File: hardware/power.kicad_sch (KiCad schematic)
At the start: 39 parts, among them J2 USB4110-GF-A, J3 B2B-PH-K-S, J4 PRPC001DAAN-RC, J5 PRPC001DAAN-RC, J6 PRPC001DAAN-RC, Q1 IRLML2246TRPBF, U1 USBLC6-2SC6, U2 BQ24074RGT, U3 TLV76733DGNR

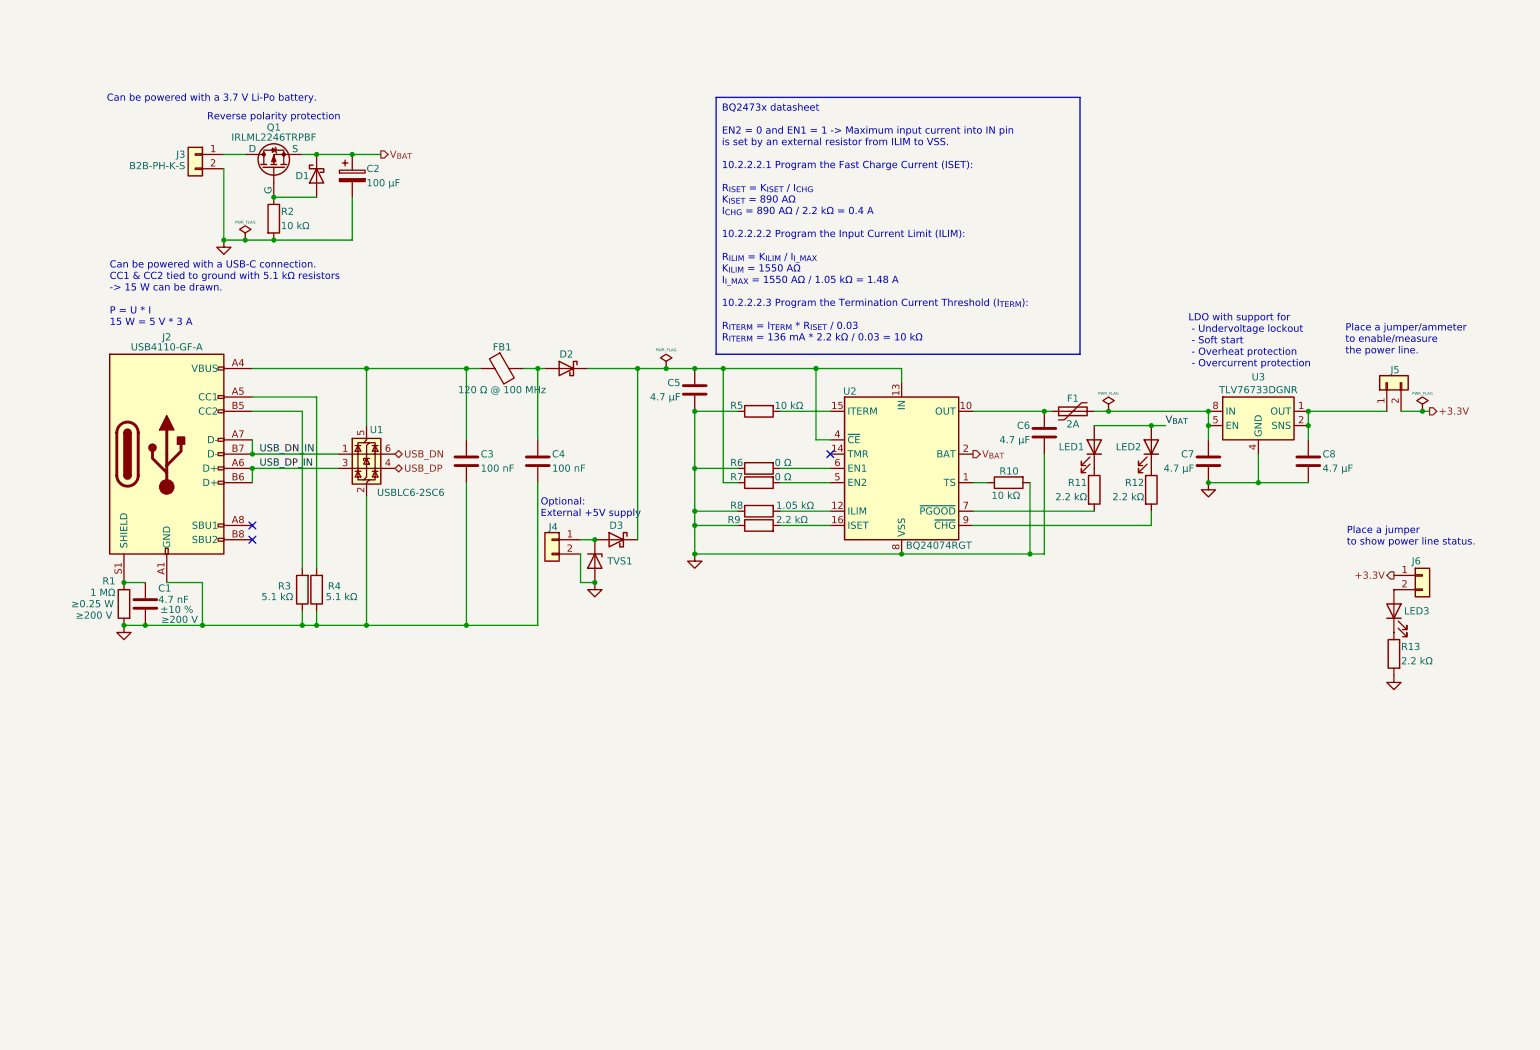
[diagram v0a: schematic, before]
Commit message: HW: Replace TC2050 wiht 10-pin connector
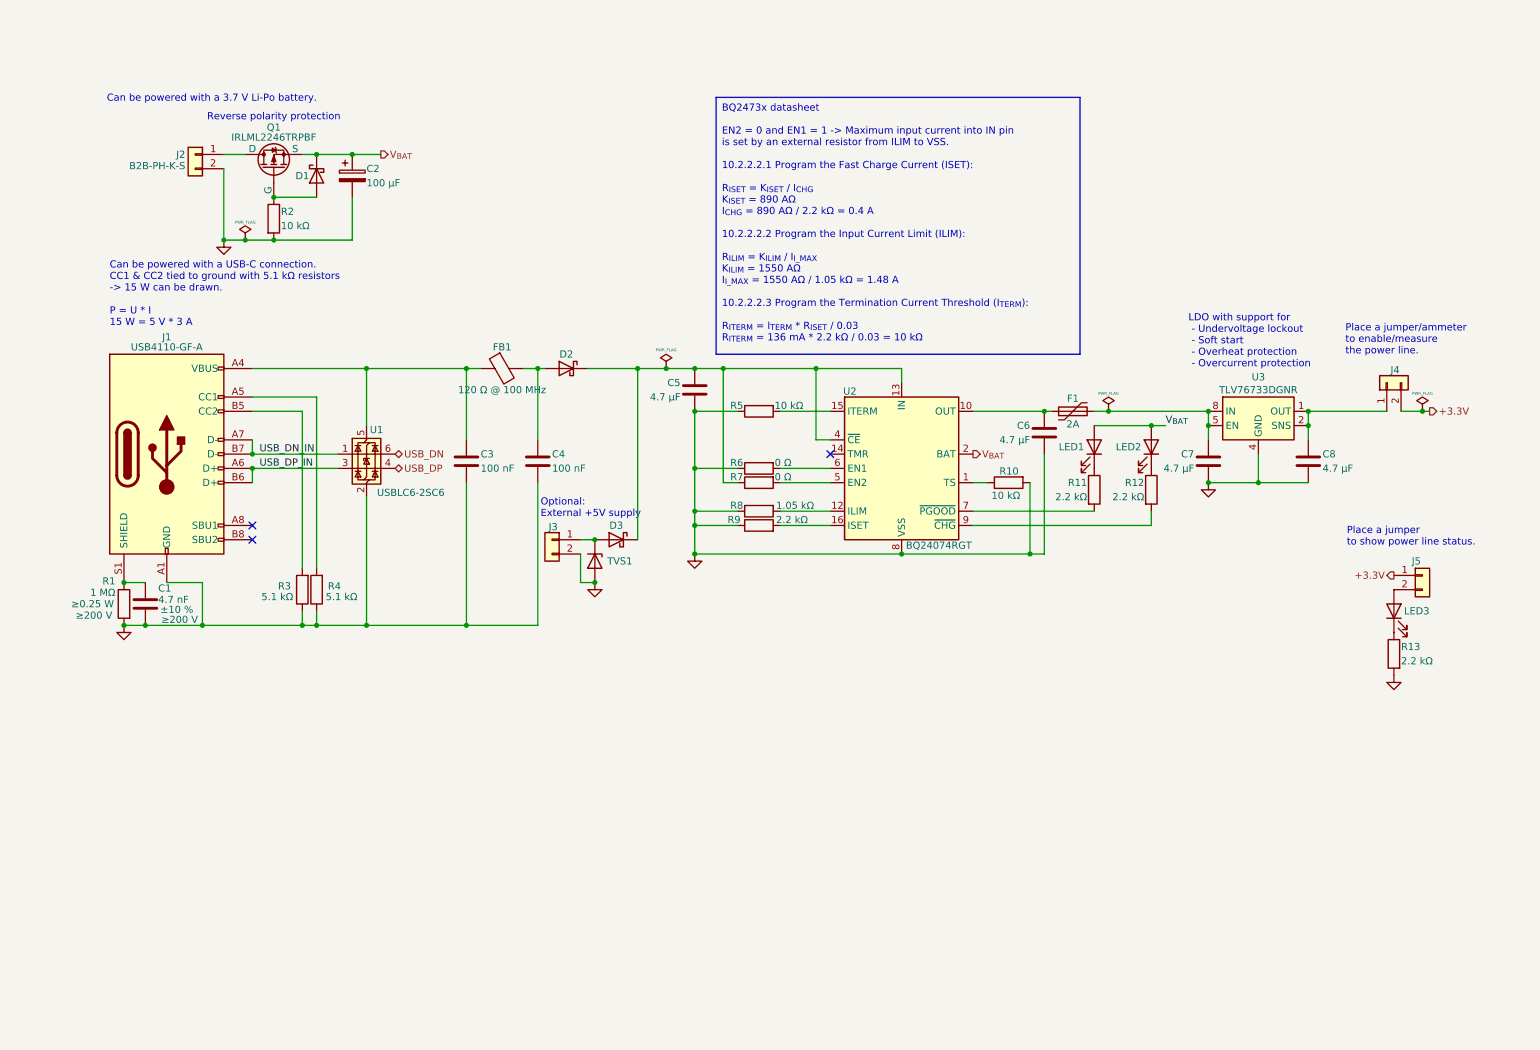
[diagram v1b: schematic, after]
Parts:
- renumbered J2 to J1, J3 to J2, J4 to J3, J5 to J4, J6 to J5
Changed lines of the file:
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@@
 		(dnp no)
 		(fields_autoplaced yes)
-		(property "Reference" "#PWR07"
+		(property "Reference" "#PWR05"
 			(at 54.61 60.96 0)
 			(effects
@@
 			(project "iida_devkit"
 				(path "/b12a6e25-97fb-4aba-bc96-af8db389bb9a/8a51e004-740e-440f-9bfb-b035bcbeb0d2"
-					(reference "#PWR07")
+					(reference "#PWR05")
 					(unit 1)
 				)
@@
 		(dnp no)
 		(fields_autoplaced yes)
-		(property "Reference" "#PWR010"
+		(property "Reference" "#PWR08"
 			(at 229.87 104.14 0)
 			(effects
@@
 			(project "iida_devkit"
 				(path "/b12a6e25-97fb-4aba-bc96-af8db389bb9a/8a51e004-740e-440f-9bfb-b035bcbeb0d2"
-					(reference "#PWR010")
+					(reference "#PWR08")
 					(unit 1)
 				)
@@
 		(on_board yes)
 		(dnp no)
-		(property "Reference" "J3"
+		(property "Reference" "J2"
 			(at 47.752 39.37 0)
 			(effects
@@
 			(project "iida_devkit"
 				(path "/b12a6e25-97fb-4aba-bc96-af8db389bb9a/8a51e004-740e-440f-9bfb-b035bcbeb0d2"
-					(reference "J3")
+					(reference "J2")
 					(unit 1)
 				)
@@
 		(on_board yes)
 		(dnp no)
-		(property "Reference" "J5"
+		(property "Reference" "J4"
 			(at 263.906 77.724 90)
 			(effects
@@
 			(project "iida_devkit"
 				(path "/b12a6e25-97fb-4aba-bc96-af8db389bb9a/8a51e004-740e-440f-9bfb-b035bcbeb0d2"
-					(reference "J5")
+					(reference "J4")
 					(unit 1)
 				)
@@
 		(on_board yes)
 		(dnp no)
-		(property "Reference" "J6"
+		(property "Reference" "J5"
 			(at 266.065 111.76 0)
 			(effects
@@
 			(project "iida_devkit"
 				(path "/b12a6e25-97fb-4aba-bc96-af8db389bb9a/8a51e004-740e-440f-9bfb-b035bcbeb0d2"
-					(reference "J6")
+					(reference "J5")
 					(unit 1)
 				)
@@
 		(dnp no)
 		(fields_autoplaced yes)
-		(property "Reference" "#PWR08"
+		(property "Reference" "#PWR06"
 			(at 120.65 121.92 0)
 			(effects
@@
 			(project "iida_devkit"
 				(path "/b12a6e25-97fb-4aba-bc96-af8db389bb9a/8a51e004-740e-440f-9bfb-b035bcbeb0d2"
-					(reference "#PWR08")
+					(reference "#PWR06")
 					(unit 1)
 				)
@@
 		(dnp no)
 		(fields_autoplaced yes)
-		(property "Reference" "#PWR09"
+		(property "Reference" "#PWR07"
 			(at 138.43 116.84 0)
 			(effects
@@
 			(project "iida_devkit"
 				(path "/b12a6e25-97fb-4aba-bc96-af8db389bb9a/8a51e004-740e-440f-9bfb-b035bcbeb0d2"
-					(reference "#PWR09")
+					(reference "#PWR07")
 					(unit 1)
 				)
@@
 		(on_board yes)
 		(dnp no)
-		(property "Reference" "J2"
+		(property "Reference" "J1"
 			(at 44.45 71.882 0)
 			(effects
@@
 			(project ""
 				(path "/b12a6e25-97fb-4aba-bc96-af8db389bb9a/8a51e004-740e-440f-9bfb-b035bcbeb0d2"
-					(reference "J2")
+					(reference "J1")
 					(unit 1)
 				)
@@
 		(on_board yes)
 		(dnp no)
-		(property "Reference" "J4"
+		(property "Reference" "J3"
 			(at 114.046 105.664 0)
 			(effects
@@
 			(project "iida_devkit"
 				(path "/b12a6e25-97fb-4aba-bc96-af8db389bb9a/8a51e004-740e-440f-9bfb-b035bcbeb0d2"
-					(reference "J4")
+					(reference "J3")
 					(unit 1)
 				)
@@
 		(dnp no)
 		(fields_autoplaced yes)
-		(property "Reference" "#PWR06"
+		(property "Reference" "#PWR04"
 			(at 36.83 129.54 0)
 			(effects
@@
 			(project "iida_devkit"
 				(path "/b12a6e25-97fb-4aba-bc96-af8db389bb9a/8a51e004-740e-440f-9bfb-b035bcbeb0d2"
-					(reference "#PWR06")
+					(reference "#PWR04")
 					(unit 1)
 				)
@@
 		(dnp no)
 		(fields_autoplaced yes)
-		(property "Reference" "#PWR011"
+		(property "Reference" "#PWR09"
 			(at 262.89 138.43 0)
 			(effects
@@
 			(project "iida_devkit"
 				(path "/b12a6e25-97fb-4aba-bc96-af8db389bb9a/8a51e004-740e-440f-9bfb-b035bcbeb0d2"
-					(reference "#PWR011")
+					(reference "#PWR09")
 					(unit 1)
 				)

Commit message: HW: Update components to be hand solderable
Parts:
- C1: footprint Capacitor_SMD:C_0805_2012Metric -> Capacitor_SMD:C_0805_2012Metric_Pad1.18x1.45mm_HandSolder
- C3, C4: footprint perfect_footprints:0402_1005_perfect -> Capacitor_SMD:C_0402_1005Metric_Pad0.74x0.62mm_HandSolder
- C5, C6, C7, C8: footprint Capacitor_SMD:C_0603_1608Metric -> Capacitor_SMD:C_0603_1608Metric_Pad1.08x0.95mm_HandSolder
- D1, D2, D3: footprint Diode_SMD:D_SMA -> Diode_SMD:D_SMA_Handsoldering
- F1: footprint Fuse:Fuse_0805_2012Metric -> Fuse:Fuse_0805_2012Metric_Pad1.15x1.40mm_HandSolder
- FB1: footprint Resistor_SMD:R_0603_1608Metric -> Resistor_SMD:R_0603_1608Metric_Pad0.98x0.95mm_HandSolder
- LED1, LED2, LED3: footprint LED_SMD:LED_PLCC_2835 -> LED_SMD:LED_PLCC_2835_Handsoldering
- Q1: footprint Package_TO_SOT_SMD:SOT-23-3 -> Package_TO_SOT_SMD:SC-59_Handsoldering
- R1: footprint Resistor_SMD:R_1206_3216Metric -> Resistor_SMD:R_1206_3216Metric_Pad1.30x1.75mm_HandSolder
- R10, R11, R12, R13, R2, R3, R4, R5, R6, R7, R8, R9: footprint perfect_footprints:0402_1005_perfect -> Resistor_SMD:R_0402_1005Metric_Pad0.72x0.64mm_HandSolder
- TVS1: footprint perfect_footprints:0402_1005_perfect -> Diode_SMD:D_0402_1005Metric_Pad0.77x0.64mm_HandSolder
- U1: footprint Package_TO_SOT_SMD:SOT-23-6 -> Package_TO_SOT_SMD:SOT-23-6_Handsoldering
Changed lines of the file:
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@@
 			)
 		)
-		(property "Footprint" "Capacitor_SMD:C_0603_1608Metric"
+		(property "Footprint" "Capacitor_SMD:C_0603_1608Metric_Pad1.08x0.95mm_HandSolder"
 			(at 248.6152 97.79 0)
 			(effects
@@
 			)
 		)
-		(property "Footprint" "LED_SMD:LED_PLCC_2835"
+		(property "Footprint" "LED_SMD:LED_PLCC_2835_Handsoldering"
 			(at 219.71 91.44 0)
 			(effects
@@
 			)
 		)
-		(property "Footprint" "perfect_footprints:0402_1005_perfect"
+		(property "Footprint" "Resistor_SMD:R_0402_1005Metric_Pad0.72x0.64mm_HandSolder"
 			(at 149.86 101.092 90)
 			(effects
@@
 			)
 		)
-		(property "Footprint" "perfect_footprints:0402_1005_perfect"
+		(property "Footprint" "Resistor_SMD:R_0402_1005Metric_Pad0.72x0.64mm_HandSolder"
 			(at 149.86 93.472 90)
 			(effects
@@
 			)
 		)
-		(property "Footprint" "Fuse:Fuse_0805_2012Metric"
+		(property "Footprint" "Fuse:Fuse_0805_2012Metric_Pad1.15x1.40mm_HandSolder"
 			(at 210.82 83.82 0)
 			(effects
@@
 			)
 		)
-		(property "Footprint" "Capacitor_SMD:C_0603_1608Metric"
+		(property "Footprint" "Capacitor_SMD:C_0603_1608Metric_Pad1.08x0.95mm_HandSolder"
 			(at 228.9048 97.79 0)
 			(effects
@@
 			)
 		)
-		(property "Footprint" "Capacitor_SMD:C_0805_2012Metric"
+		(property "Footprint" "Capacitor_SMD:C_0805_2012Metric_Pad1.18x1.45mm_HandSolder"
 			(at 41.6052 123.19 0)
 			(effects
@@
 			)
 		)
-		(property "Footprint" "perfect_footprints:0402_1005_perfect"
+		(property "Footprint" "Capacitor_SMD:C_0402_1005Metric_Pad0.74x0.62mm_HandSolder"
 			(at 111.4552 97.79 0)
 			(effects
@@
 			)
 		)
-		(property "Footprint" "perfect_footprints:0402_1005_perfect"
+		(property "Footprint" "Resistor_SMD:R_0402_1005Metric_Pad0.72x0.64mm_HandSolder"
 			(at 61.722 50.8 90)
 			(effects
@@
 			)
 		)
-		(property "Footprint" "Package_TO_SOT_SMD:SOT-23-6"
+		(property "Footprint" "Package_TO_SOT_SMD:SOT-23-6_Handsoldering"
 			(at 80.01 105.41 0)
 			(effects
@@
 			)
 		)
-		(property "Footprint" "perfect_footprints:0402_1005_perfect"
+		(property "Footprint" "Resistor_SMD:R_0402_1005Metric_Pad0.72x0.64mm_HandSolder"
 			(at 149.86 96.012 90)
 			(effects
@@
 			)
 		)
-		(property "Footprint" "perfect_footprints:0402_1005_perfect"
+		(property "Footprint" "Resistor_SMD:R_0402_1005Metric_Pad0.72x0.64mm_HandSolder"
 			(at 149.86 107.188 90)
 			(effects
@@
 			)
 		)
-		(property "Footprint" "Capacitor_SMD:C_0603_1608Metric"
+		(property "Footprint" "Capacitor_SMD:C_0603_1608Metric_Pad1.08x0.95mm_HandSolder"
 			(at 137.4648 85.09 0)
 			(effects
@@
 			)
 		)
-		(property "Footprint" "perfect_footprints:0402_1005_perfect"
+		(property "Footprint" "Resistor_SMD:R_0402_1005Metric_Pad0.72x0.64mm_HandSolder"
 			(at 194.31 96.012 90)
 			(effects
@@
 			)
 		)
-		(property "Footprint" "LED_SMD:LED_PLCC_2835"
+		(property "Footprint" "LED_SMD:LED_PLCC_2835_Handsoldering"
 			(at 209.55 91.44 0)
 			(effects
@@
 			)
 		)
-		(property "Footprint" "Resistor_SMD:R_1206_3216Metric"
+		(property "Footprint" "Resistor_SMD:R_1206_3216Metric_Pad1.30x1.75mm_HandSolder"
 			(at 38.608 119.38 90)
 			(effects
@@
 			)
 		)
-		(property "Footprint" "perfect_footprints:0402_1005_perfect"
+		(property "Footprint" "Capacitor_SMD:C_0402_1005Metric_Pad0.74x0.62mm_HandSolder"
 			(at 98.7552 97.79 0)
 			(effects
@@
 			)
 		)
-		(property "Footprint" "perfect_footprints:0402_1005_perfect"
+		(property "Footprint" "Resistor_SMD:R_0402_1005Metric_Pad0.72x0.64mm_HandSolder"
 			(at 207.772 99.06 90)
 			(effects
@@
 			)
 		)
-		(property "Footprint" "perfect_footprints:0402_1005_perfect"
+		(property "Footprint" "Resistor_SMD:R_0402_1005Metric_Pad0.72x0.64mm_HandSolder"
 			(at 264.668 128.27 90)
 			(effects
@@
 			)
 		)
-		(property "Footprint" "Resistor_SMD:R_0603_1608Metric"
+		(property "Footprint" "Resistor_SMD:R_0603_1608Metric_Pad0.98x0.95mm_HandSolder"
 			(at 104.14 75.692 90)
 			(effects
@@
 			)
 		)
-		(property "Footprint" "Capacitor_SMD:C_0603_1608Metric"
+		(property "Footprint" "Capacitor_SMD:C_0603_1608Metric_Pad1.08x0.95mm_HandSolder"
 			(at 199.6948 92.71 0)
 			(effects
@@
 			)
 		)
-		(property "Footprint" "perfect_footprints:0402_1005_perfect"
+		(property "Footprint" "Diode_SMD:D_0402_1005Metric_Pad0.77x0.64mm_HandSolder"
 			(at 120.65 111.76 0)
 			(effects
@@
 			)
 		)
-		(property "Footprint" "perfect_footprints:0402_1005_perfect"
+		(property "Footprint" "Resistor_SMD:R_0402_1005Metric_Pad0.72x0.64mm_HandSolder"
 			(at 217.932 99.06 90)
 			(effects
@@
 			)
 		)
-		(property "Footprint" "Package_TO_SOT_SMD:SOT-23-3"
+		(property "Footprint" "Package_TO_SOT_SMD:SC-59_Handsoldering"
 			(at 60.96 36.83 0)
 			(effects
@@
 			)
 		)
-		(property "Footprint" "perfect_footprints:0402_1005_perfect"
+		(property "Footprint" "Resistor_SMD:R_0402_1005Metric_Pad0.72x0.64mm_HandSolder"
 			(at 72.898 116.84 90)
 			(effects
@@
 			)
 		)
-		(property "Footprint" "perfect_footprints:0402_1005_perfect"
+		(property "Footprint" "Resistor_SMD:R_0402_1005Metric_Pad0.72x0.64mm_HandSolder"
 			(at 70.358 116.84 90)
 			(effects
@@
 			)
 		)
-		(property "Footprint" "Diode_SMD:D_SMA"
+		(property "Footprint" "Diode_SMD:D_SMA_Handsoldering"
 			(at 71.12 43.18 0)
 			(effects
@@
 			)
 		)
-		(property "Footprint" "perfect_footprints:0402_1005_perfect"
+		(property "Footprint" "Resistor_SMD:R_0402_1005Metric_Pad0.72x0.64mm_HandSolder"
 			(at 149.86 83.312 90)
 			(effects
@@
 			)
 		)
-		(property "Footprint" "LED_SMD:LED_PLCC_2835"
+		(property "Footprint" "LED_SMD:LED_PLCC_2835_Handsoldering"
 			(at 262.89 120.65 0)
 			(effects
@@
 			)
 		)
-		(property "Footprint" "Diode_SMD:D_SMA"
+		(property "Footprint" "Diode_SMD:D_SMA_Handsoldering"
 			(at 115.57 77.47 0)
 			(effects
@@
 			)
 		)
-		(property "Footprint" "Diode_SMD:D_SMA"
+		(property "Footprint" "Diode_SMD:D_SMA_Handsoldering"
 			(at 124.46 107.95 0)
 			(effects
